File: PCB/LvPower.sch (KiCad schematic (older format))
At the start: 34 parts

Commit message: Add missing footprints
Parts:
- NT? (x2): footprint (none) -> Parts:NetTie-2
- U?: footprint Parts:WSON6-PAD -> Parts:WSON6-2x2-PAD
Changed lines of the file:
@@
 F 0 "NT?" H 4050 3531 50  0000 C CNN
 F 1 "Net-Tie_2" H 4050 3440 50  0000 C CNN
-F 2 "" H 4050 3350 50  0001 C CNN
+F 2 "Parts:NetTie-2" H 4050 3350 50  0001 C CNN
 F 3 "~" H 4050 3350 50  0001 C CNN
 	1    4050 3350
@@
 F 0 "NT?" H 4050 5681 50  0000 C CNN
 F 1 "Net-Tie_2" H 4050 5590 50  0000 C CNN
-F 2 "" H 4050 5500 50  0001 C CNN
+F 2 "Parts:NetTie-2" H 4050 5500 50  0001 C CNN
 F 3 "~" H 4050 5500 50  0001 C CNN
 	1    4050 5500
@@
 F 0 "U?" H 4050 5387 60  0000 C CNN
 F 1 "TPS62262" H 4050 5281 60  0000 C CNN
-F 2 "Parts:WSON6-PAD" H 4050 4650 60  0001 C CNN
+F 2 "Parts:WSON6-2x2-PAD" H 4050 4650 60  0001 C CNN
 F 3 "http://www.ti.com/product/TPS62262" H 3650 5000 60  0001 C CNN
 	1    4050 4950

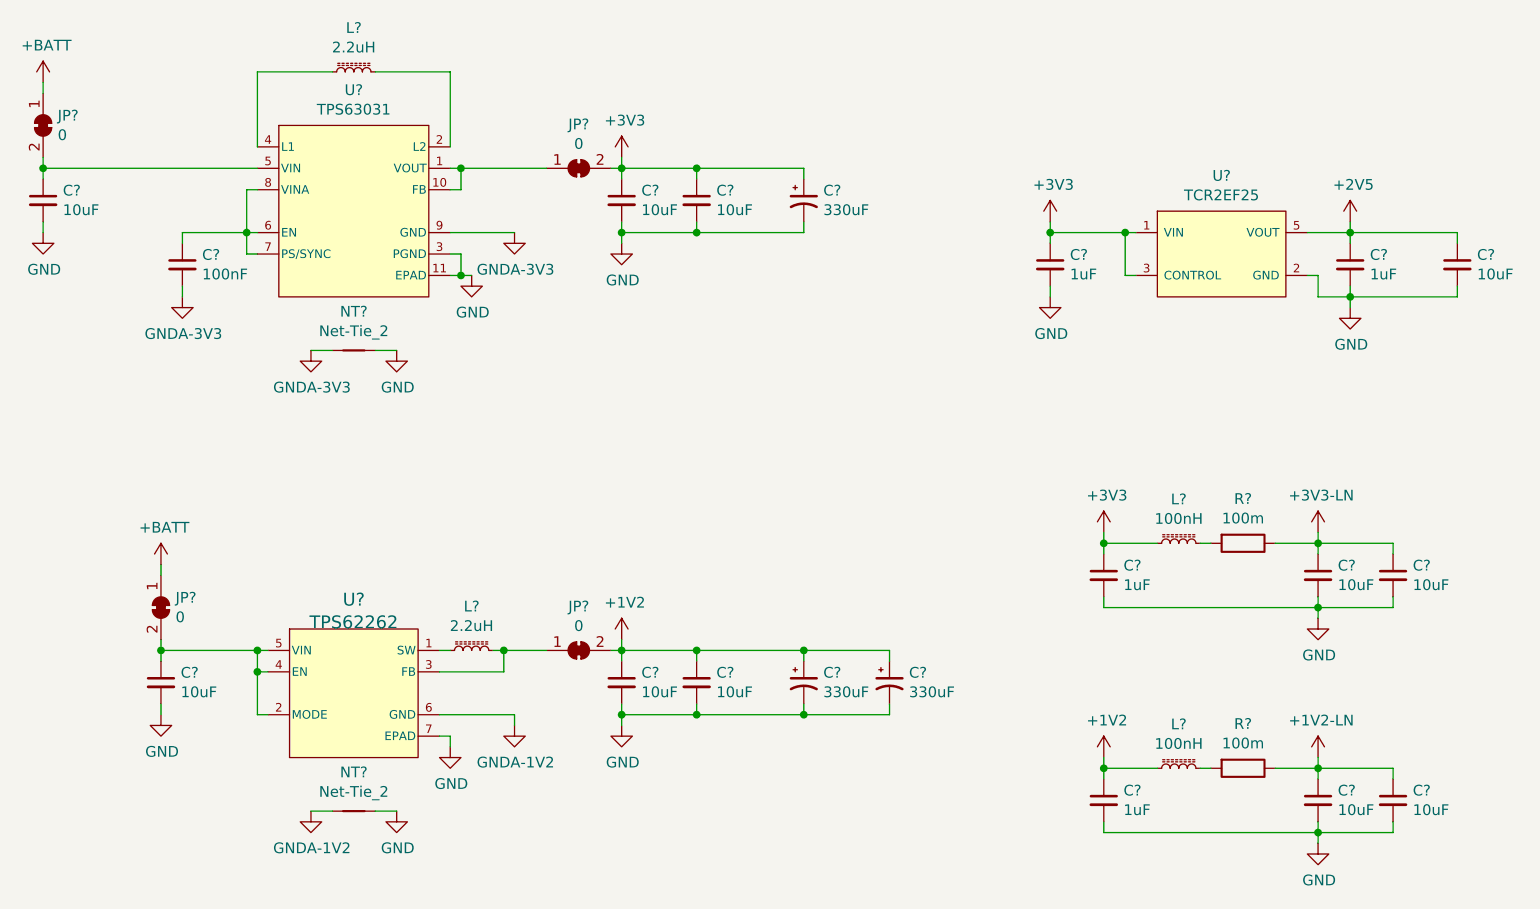
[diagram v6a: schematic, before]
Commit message: Annotate schematic, simplify transmit circuit, shuffle receive opamp stages, reorder buttons so they match net names, reorder connectors to simplify routing, begin arranging parts on PCB
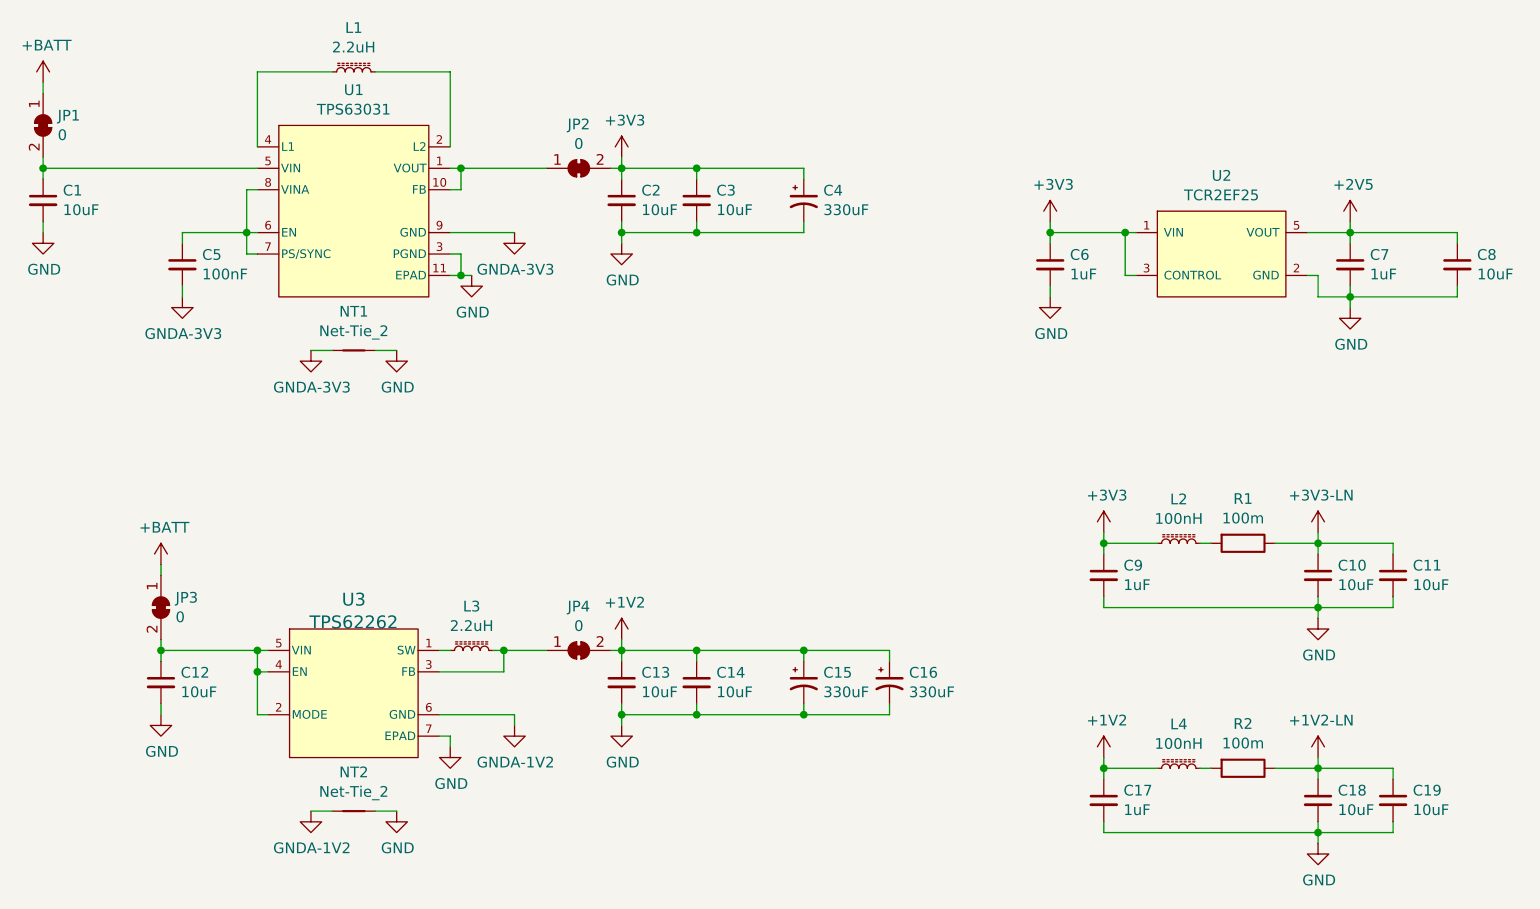
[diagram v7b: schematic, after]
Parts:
- gave numbers to parts that had none: 34
